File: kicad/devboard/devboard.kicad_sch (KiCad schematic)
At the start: 32 parts, among them J1 USB_C_Receptacle, J2 Conn_01x04_Socket, SW1 SW_DIP_x04, U1 LM3940, U2 CH340G, U3 STM32G030K8Tx, Y1 12 MHz, Y2 8 MHz

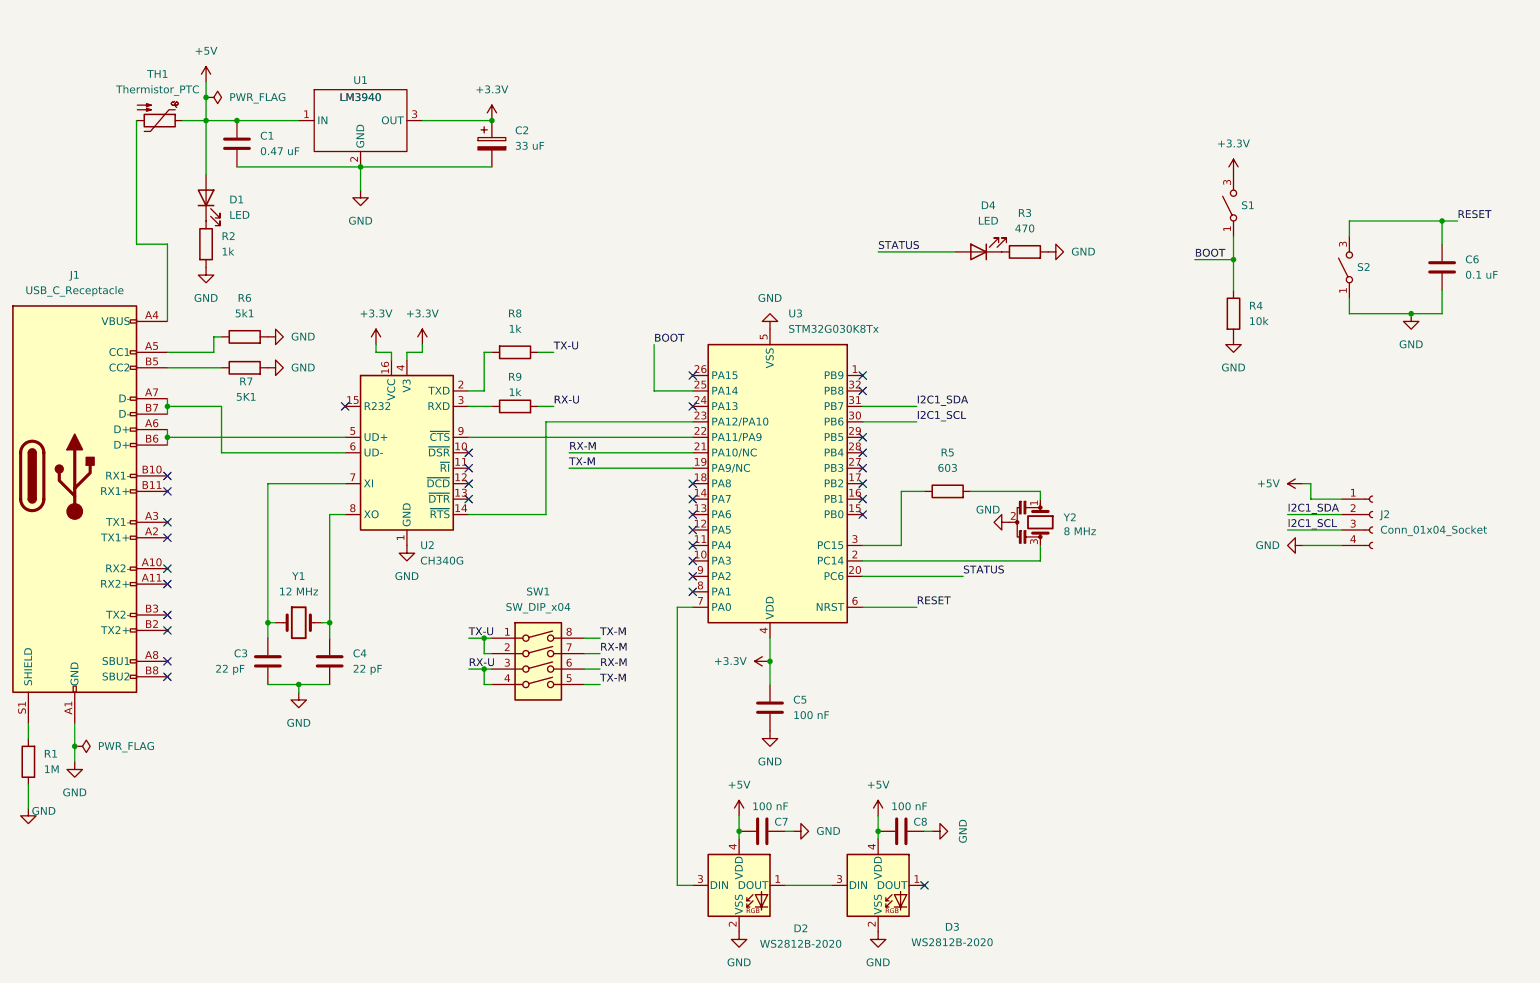
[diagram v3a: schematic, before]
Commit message: Added pin headers for SWD
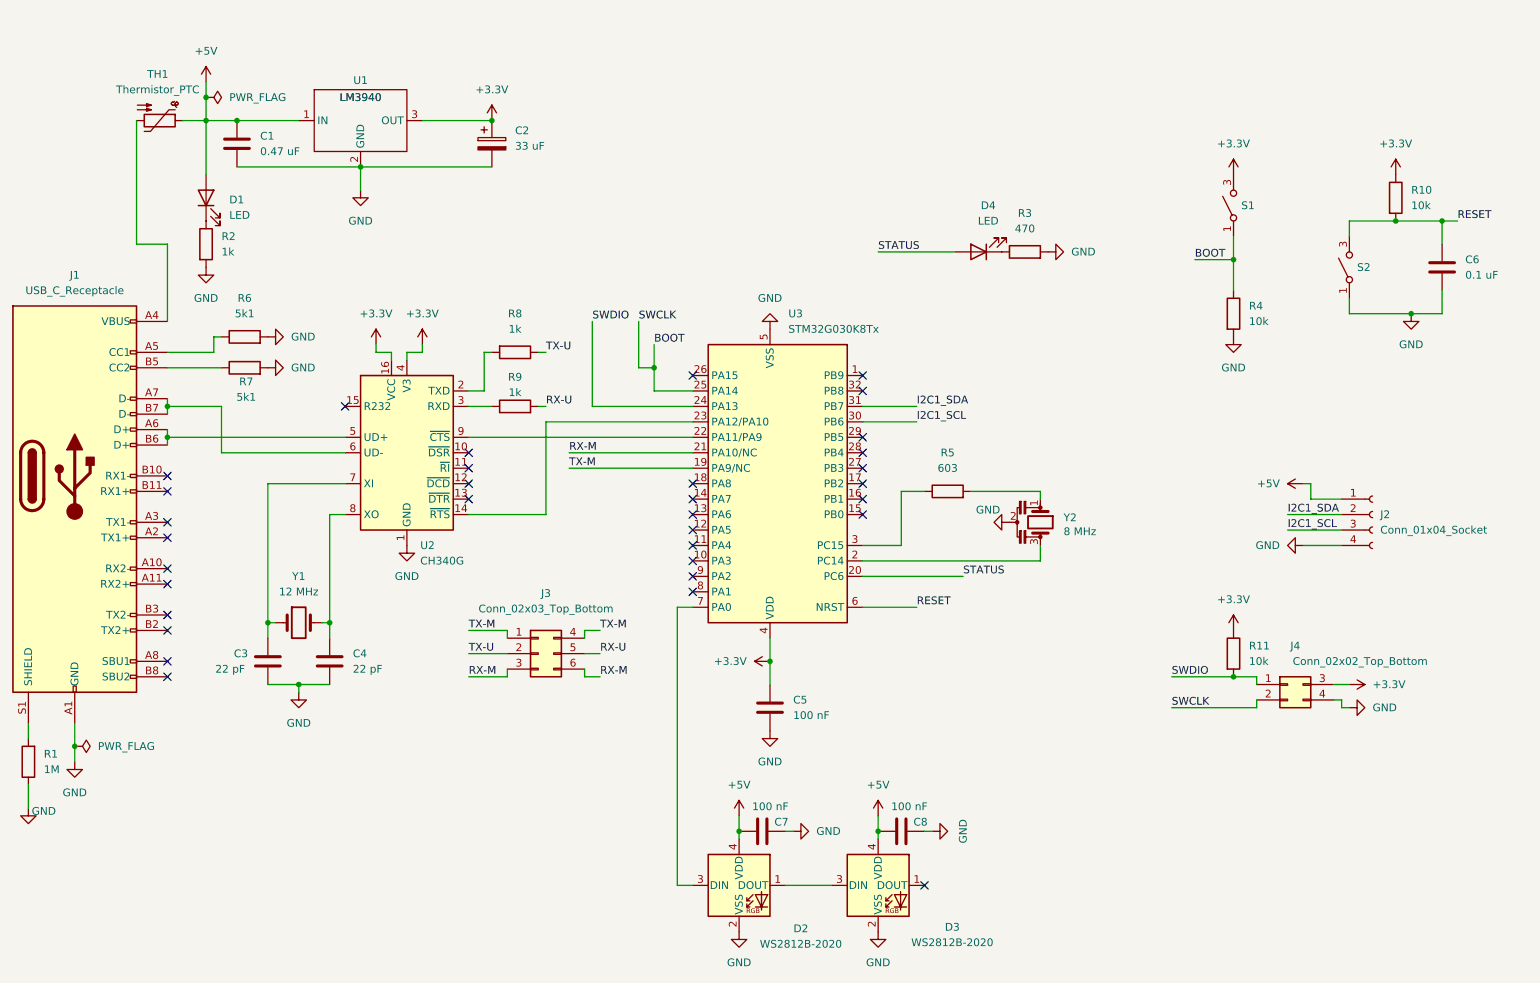
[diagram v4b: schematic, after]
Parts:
- removed SW1: SW_DIP_x04, Button_Switch_SMD:SW_DIP_SPSTx04_Slide_9.78x12.34mm_W8.61mm_P2.54mm, symbol Switch:SW_DIP_x04
- added J3: Conn_02x03_Top_Bottom, Connector_PinHeader_2.54mm:PinHeader_2x03_P2.54mm_Vertical, symbol Connector_Generic:Conn_02x03_Top_Bottom
- added J4: Conn_02x02_Top_Bottom, Connector_PinHeader_2.54mm:PinHeader_2x02_P2.54mm_Vertical, symbol Connector_Generic:Conn_02x02_Top_Bottom
- added R10, R11: 10k, Resistor_SMD:R_0603_1608Metric, symbol Device:R
- J2: footprint Connector_PinHeader_1.00mm:PinHeader_1x04_P1.00mm_Vertical -> Connector_PinHeader_2.54mm:PinHeader_1x04_P2.54mm_Vertical
- R7: value 5K1 -> 5k1
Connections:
- net +3.3V: now also J4.3 (Pin_3), R10.1, R11.1
- net BOOT: now also J4.2 (Pin_2)
- net GND: now also J4.4 (Pin_4)
- net RESET: now also R10.2
- net RX-M: now also J3.3 (Pin_3), J3.6 (Pin_6)
- net RX-U: now also J3.5 (Pin_5)
- net TX-M: now also J3.1 (Pin_1), J3.4 (Pin_4)
- net TX-U: now also J3.2 (Pin_2)
- net SWDIO: now reaches U3.24 (PA13)
- net SWDIO: now also J4.1 (Pin_1), R11.2
- no-connect marks 34 -> 33

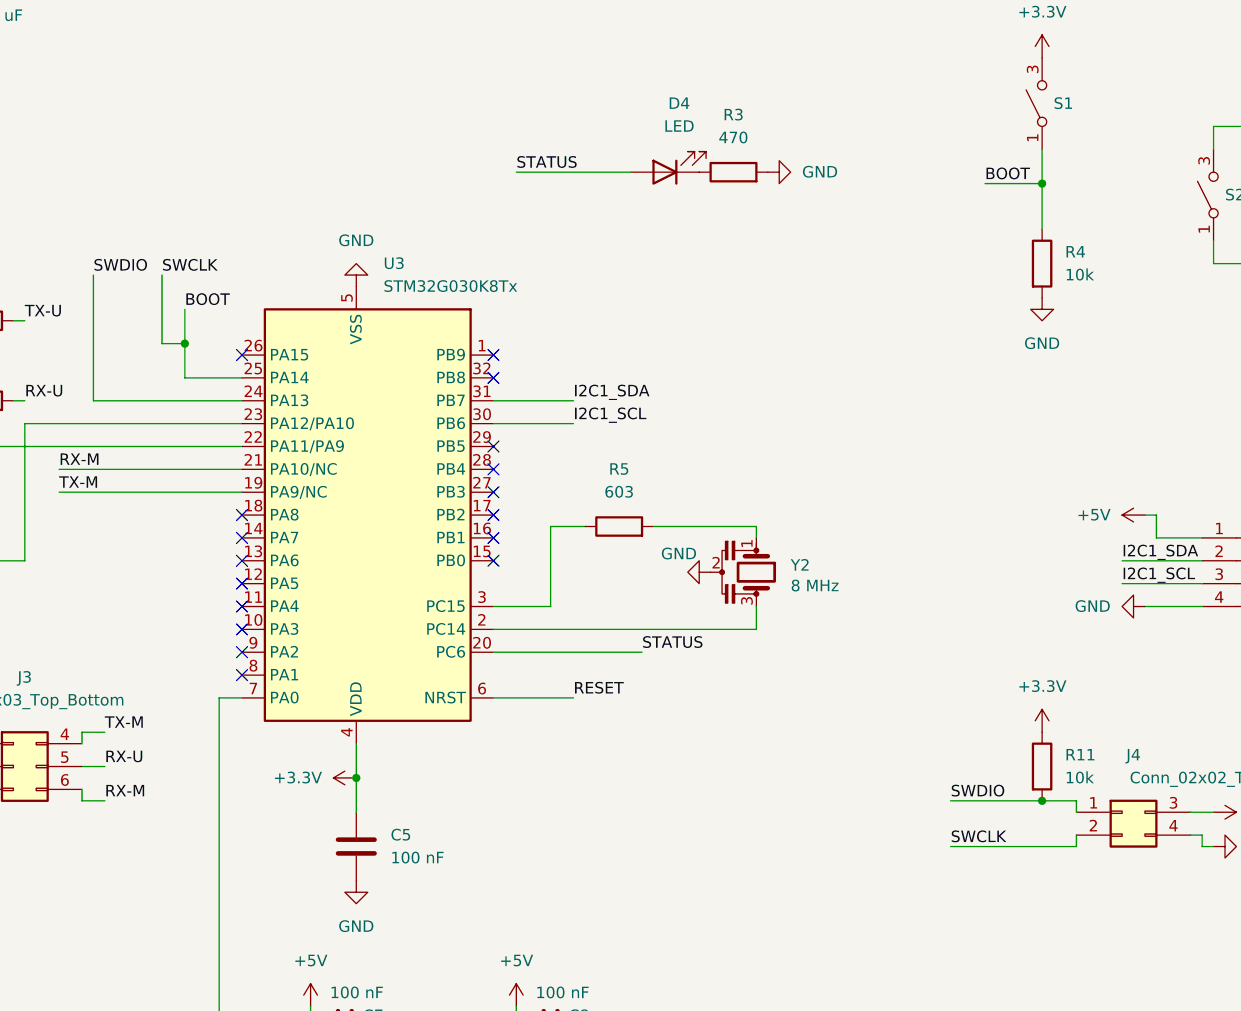
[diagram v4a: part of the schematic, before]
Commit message: Updated boot/swclk net name
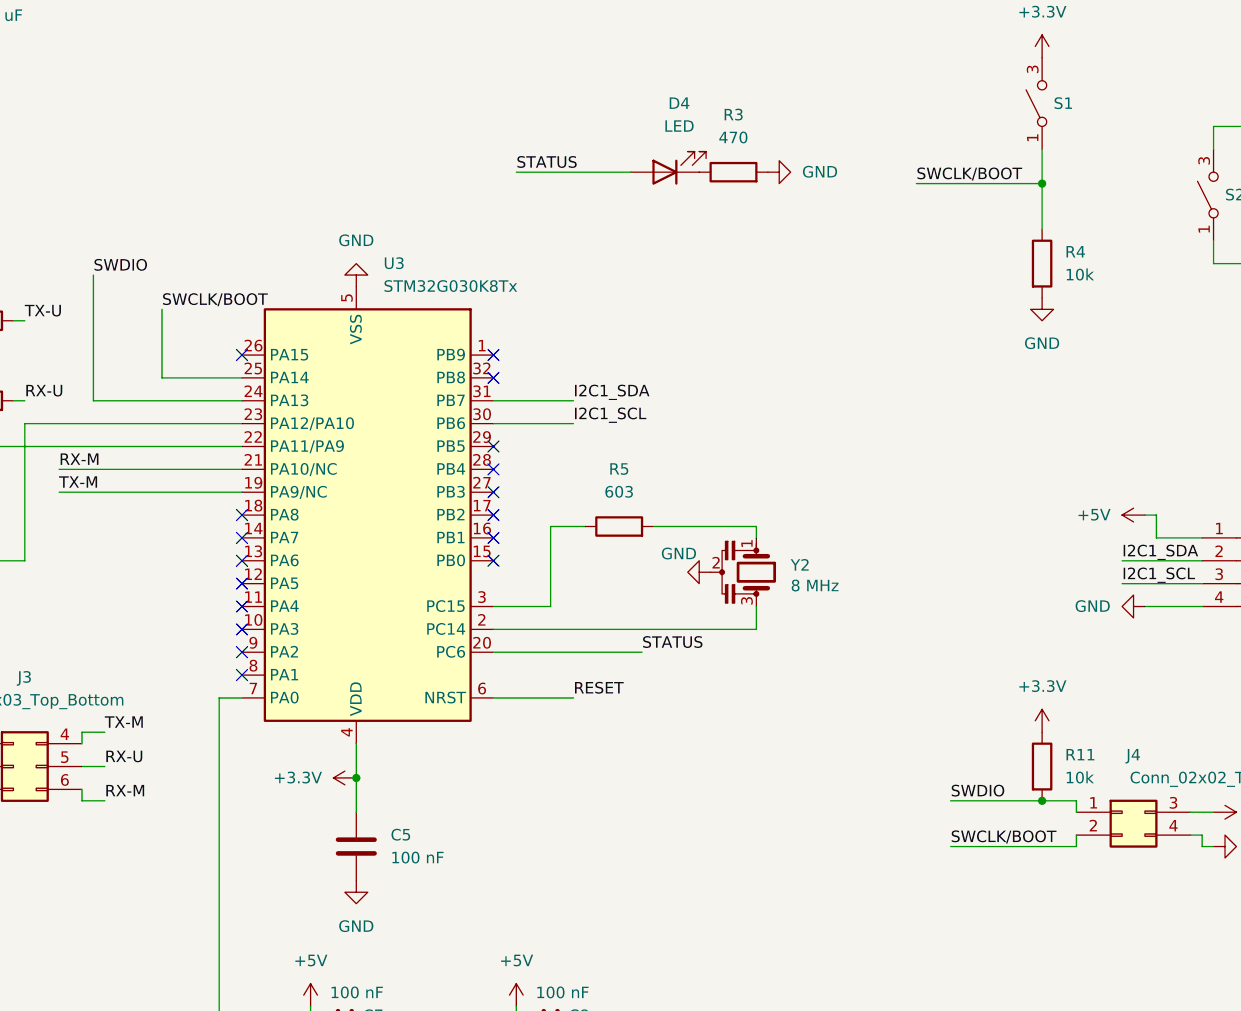
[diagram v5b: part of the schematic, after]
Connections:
- net BOOT renamed SWCLK/BOOT
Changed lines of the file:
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@@
-	)
-	(junction
-		(at 124.46 72.39)
-		(diameter 0)
-		(color 0 0 0 0)
 	)
 	(junction
@@
 	(wire
 		(pts
-			(xy 124.46 72.39) (xy 121.92 72.39)
-		)
-		(stroke
-			(width 0)
-			(type default)
-		)
-	)
-	(wire
-		(pts
 			(xy 232.41 91.44) (xy 232.41 93.98)
 		)
@@
 	(wire
 		(pts
-			(xy 124.46 68.58) (xy 124.46 72.39)
-		)
-		(stroke
-			(width 0)
-			(type default)
-		)
-	)
-	(wire
-		(pts
 			(xy 238.76 128.27) (xy 237.49 128.27)
 		)
@@
 	(wire
 		(pts
-			(xy 121.92 64.77) (xy 121.92 72.39)
-		)
-		(stroke
-			(width 0)
-			(type default)
-		)
-	)
-	(wire
-		(pts
 			(xy 231.14 101.6) (xy 237.49 101.6)
 		)
@@
 	(wire
 		(pts
-			(xy 130.81 76.2) (xy 124.46 76.2)
-		)
-		(stroke
-			(width 0)
-			(type default)
-		)
-	)
-	(wire
-		(pts
-			(xy 213.36 54.61) (xy 219.71 54.61)
+			(xy 130.81 76.2) (xy 121.92 76.2)
+		)
+		(stroke
+			(width 0)
+			(type default)
+		)
+	)
+	(wire
+		(pts
+			(xy 205.74 54.61) (xy 219.71 54.61)
 		)
 		(stroke
@@
 	(wire
 		(pts
-			(xy 124.46 72.39) (xy 124.46 76.2)
+			(xy 121.92 68.58) (xy 121.92 76.2)
 		)
 		(stroke
@@
 		)
 	)
-	(label "SWCLK"
-		(at 121.92 64.77 0)
-		(fields_autoplaced yes)
-		(effects
-			(font
-				(size 1.27 1.27)
-			)
-			(justify left bottom)
-		)
-	)
-	(label "SWCLK"
+	(label "SWCLK{slash}BOOT"
 		(at 209.55 128.27 0)
 		(fields_autoplaced yes)
@@
 		)
 	)
-	(label "BOOT"
-		(at 213.36 54.61 0)
+	(label "SWCLK{slash}BOOT"
+		(at 205.74 54.61 0)
 		(fields_autoplaced yes)
 		(effects
@@
 		)
 	)
-	(label "BOOT"
-		(at 124.46 68.58 0)
-		(fields_autoplaced yes)
-		(effects
+	(label "SWCLK{slash}BOOT"
+		(at 121.92 68.58 0)
+		(fields_autoplaced yes)
+		(effects
